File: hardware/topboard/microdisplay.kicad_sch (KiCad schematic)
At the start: 53 parts

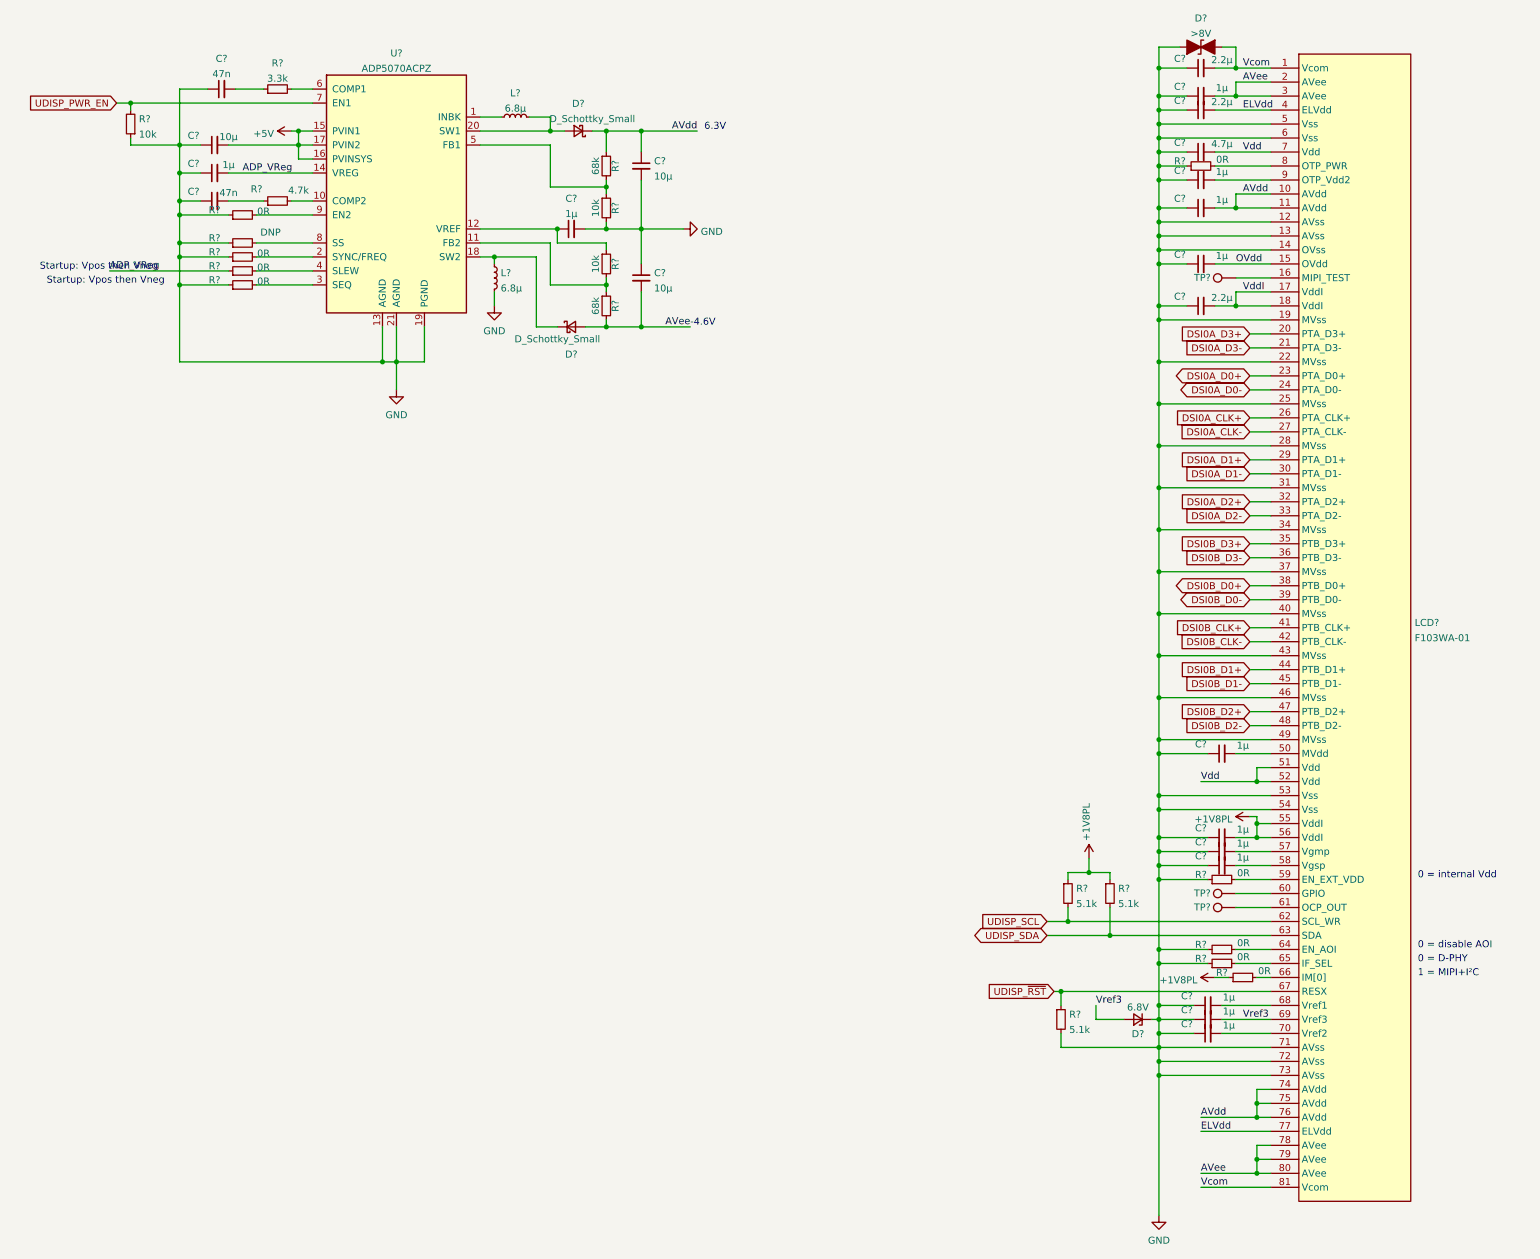
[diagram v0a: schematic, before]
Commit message: Fixing various top board issues
Signed-off-by: gatecat <gatecat@ds0.me>
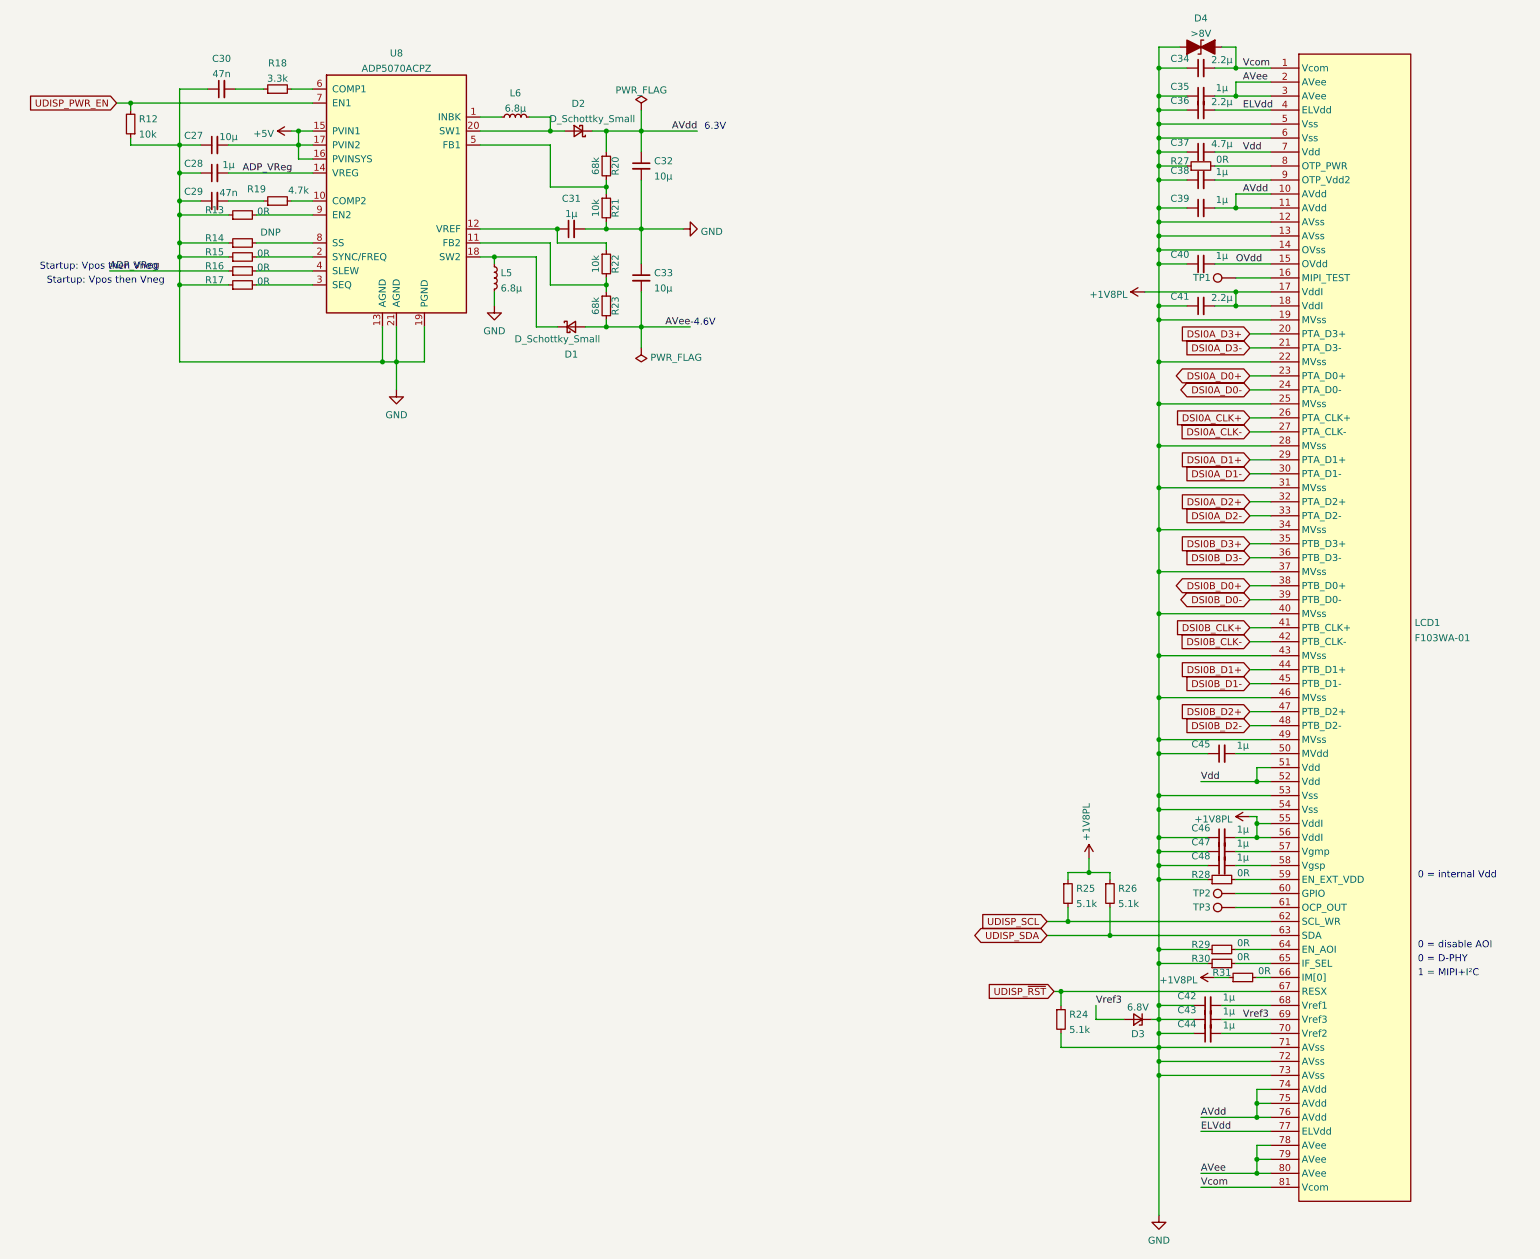
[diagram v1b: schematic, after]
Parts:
- gave numbers to parts that had none: 53
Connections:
- net VddI is gone; now on net +1V8PL: C41.2, LCD1.17 (VddI), LCD1.18 (VddI)

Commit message: Assign most top-board footprints
Signed-off-by: gatecat <gatecat@ds0.me>
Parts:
- C27, C32, C33, C37: footprint (none) -> Capacitor_SMD:C_0805_2012Metric
- C28, C31, C34, C35, C36, C38, C39, C40, C41, C42, C43, C44, C45, C46, C47, C48: footprint (none) -> Capacitor_SMD:C_0603_1608Metric
- C29, C30: footprint (none) -> Capacitor_SMD:C_0402_1005Metric
- D1, D2, D3, D4: footprint (none) -> Diode_SMD:D_SMA
- L5, L6: footprint (none) -> Inductor_SMD:L_Taiyo-Yuden_NR-50xx
- LCD1: footprint (none) -> meowality:FF0881SA1
- R12, R13, R14, R15, R16, R17, R18, R19, R20, R21, R22, R23, R24, R25, R26, R27, R28, R29, R30, R31: footprint (none) -> Resistor_SMD:R_0402_1005Metric
- TP1, TP2, TP3: footprint (none) -> TestPoint:TestPoint_Pad_D1.5mm
- U8: footprint (none) -> Package_DFN_QFN:QFN-20-1EP_4x4mm_P0.5mm_EP2.6x2.6mm
